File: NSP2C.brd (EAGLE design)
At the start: 72.1 x 82.5 mm, 15 parts, among them Q1 600mA/40V, Q2 IRF540

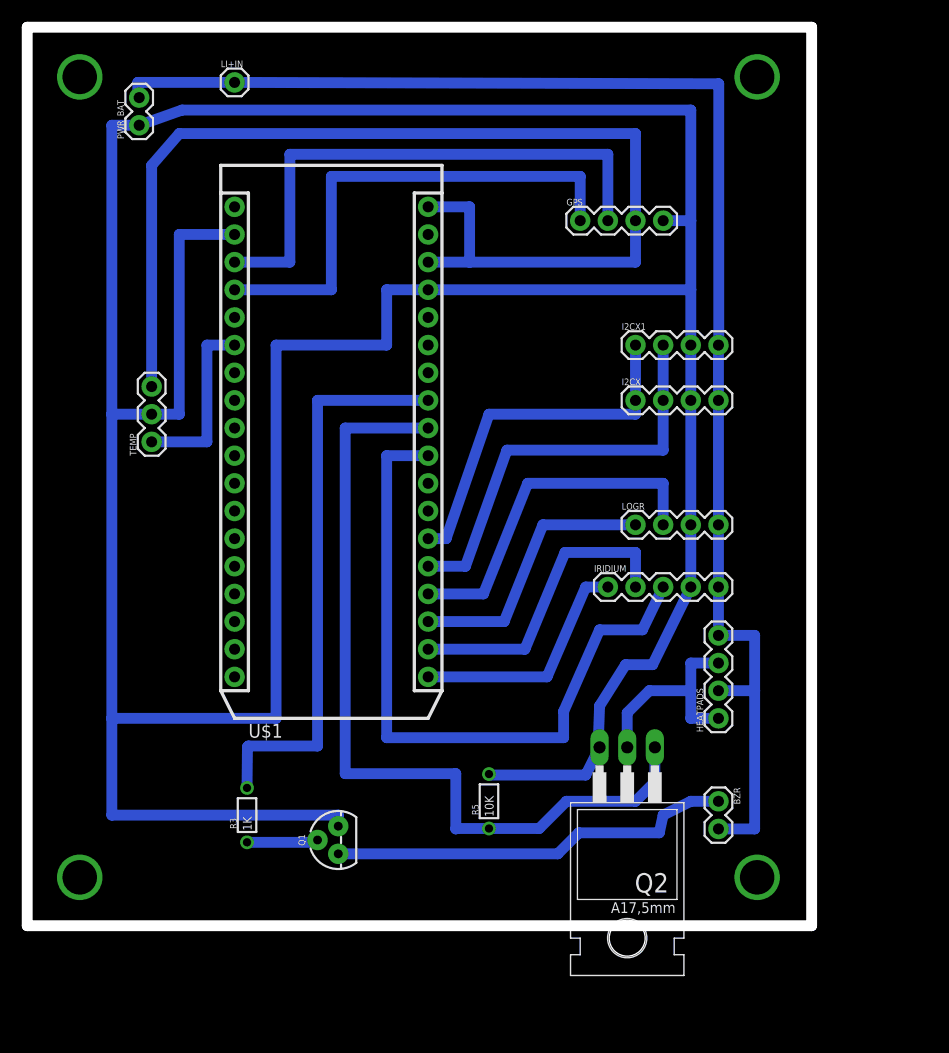
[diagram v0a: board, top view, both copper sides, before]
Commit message: Improved routing
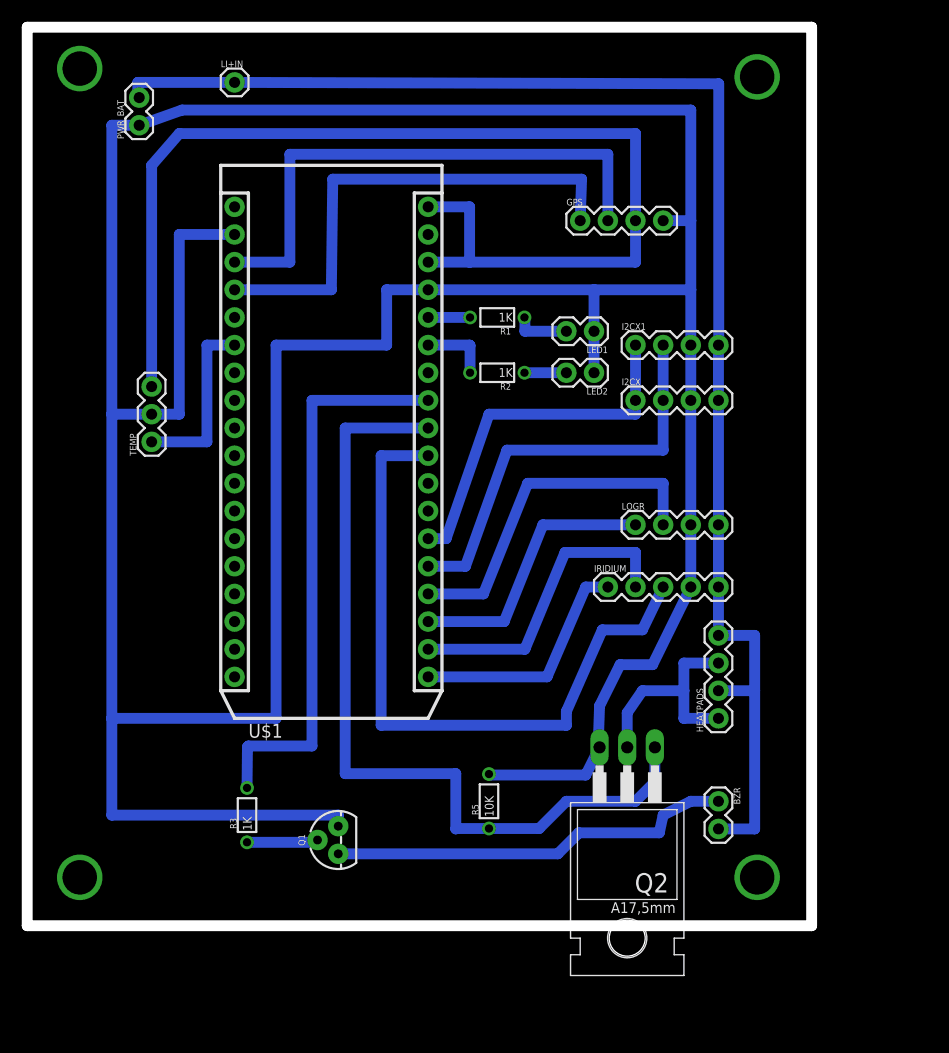
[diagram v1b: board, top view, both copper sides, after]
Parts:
- added LED1, LED2: (no value), SparkFun-Connectors:1X02
- added R1, R2: 1K, SparkFun-Passives:1/6W-RES
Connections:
- new net N$13: R2.2, U$1.31
- new net N$16: LED2.2, R2.1
- new net N$3: R1.2, U$1.32
- new net N$8: LED1.2, R1.1
- net GND: now also LED1.1, LED2.1
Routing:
- net GND: track 336.8 -> 344.6 mm
- net N$13: track 0.00 -> 6.37 mm
- net N$8: track 0.00 -> 5.10 mm
- net N$3: track 0.00 -> 3.85 mm
- net N$16: track 0.00 -> 3.85 mm
- net IRWKP: track 64.9 -> 63.6 mm
- net N$11: track 20.1 -> 21.0 mm
- net N$12: track 46.2 -> 45.7 mm
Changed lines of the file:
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@@
 <element name="Q2" library="transistor-fet" library_urn="urn:adsk.eagle:library:396" package="TO220" package3d_urn="urn:adsk.eagle:package:28520/1" value="IRF540" x="44.958" y="15.113" rot="R180"/>
 <element name="R5" library="SparkFun-Passives" package="1/6W-RES" value="10K" x="32.258" y="16.51" rot="R90"/>
+<element name="R1" library="SparkFun-Passives" package="1/6W-RES" value="1K" x="33.02" y="60.96" rot="R180"/>
+<element name="LED1" library="SparkFun-Connectors" package="1X02" value="" x="41.91" y="59.69" rot="R180"/>
+<element name="LED2" library="SparkFun-Connectors" package="1X02" value="" x="41.91" y="55.88" rot="R180"/>
+<element name="R2" library="SparkFun-Passives" package="1/6W-RES" value="1K" x="33.02" y="55.88" rot="R180"/>
 </elements>
 <signals>
@@
 <wire x1="12.7" y1="24.13" x2="-2.3876" y2="24.13" width="1" layer="16"/>
 <wire x1="22.86" y1="63.5" x2="26.67" y2="63.5" width="1" layer="16"/>
-<wire x1="26.67" y1="63.5" x2="50.8" y2="63.5" width="1" layer="16"/>
+<wire x1="41.91" y1="63.5" x2="50.8" y2="63.5" width="1" layer="16"/>
+<wire x1="41.91" y1="63.5" x2="26.67" y2="63.5" width="1" layer="16"/>
 <wire x1="50.8" y1="63.5" x2="50.8" y2="69.85" width="1" layer="16"/>
 <contactref element="GPS" pad="4"/>
@@
 <wire x1="0.127" y1="78.613" x2="-2.3876" y2="78.613" width="1" layer="16"/>
 <wire x1="-2.3876" y1="78.613" x2="-2.3876" y2="52.07" width="1" layer="16"/>
-<wire x1="47.291765625" y1="29.061590625" x2="44.809590625" y2="29.061590625" width="1" layer="16"/>
-<wire x1="44.809590625" y1="29.061590625" x2="42.418" y2="25.273" width="1" layer="16"/>
+<wire x1="47.291765625" y1="29.061590625" x2="44.301590625" y2="29.061590625" width="1" layer="16"/>
+<wire x1="44.301590625" y1="29.061590625" x2="42.418" y2="25.273" width="1" layer="16"/>
 <wire x1="42.418" y1="25.273" x2="42.291" y2="21.59" width="1" layer="16"/>
 <wire x1="42.291" y1="21.59" x2="42.418" y2="21.463" width="1" layer="16"/>
+<contactref element="LED1" pad="1"/>
+<contactref element="LED2" pad="1"/>
+<wire x1="41.91" y1="55.88" x2="41.91" y2="59.69" width="1" layer="16"/>
+<wire x1="41.91" y1="59.69" x2="41.91" y2="63.5" width="1" layer="16"/>
 </signal>
 <signal name="3.3V">
@@
 <contactref element="U$1" pad="27"/>
 <contactref element="IRIDIUM" pad="3"/>
-<wire x1="26.67" y1="48.26" x2="22.86" y2="48.26" width="1" layer="16"/>
-<wire x1="22.86" y1="48.26" x2="22.86" y2="22.352" width="1" layer="16"/>
-<wire x1="22.86" y1="22.352" x2="39.116" y2="22.352" width="1" layer="16"/>
+<wire x1="26.67" y1="48.26" x2="22.352" y2="48.26" width="1" layer="16"/>
+<wire x1="22.352" y1="48.26" x2="22.352" y2="23.495" width="1" layer="16"/>
+<wire x1="22.352" y1="23.495" x2="39.37" y2="23.495" width="1" layer="16"/>
 <wire x1="46.355" y1="32.258" x2="48.26" y2="36.195" width="1" layer="16"/>
-<wire x1="39.116" y1="22.352" x2="39.116" y2="24.765" width="1" layer="16"/>
-<wire x1="39.116" y1="24.765" x2="42.418" y2="32.258" width="1" layer="16"/>
-<wire x1="42.418" y1="32.258" x2="46.355" y2="32.258" width="1" layer="16"/>
+<wire x1="39.37" y1="23.495" x2="39.37" y2="24.765" width="1" layer="16"/>
+<wire x1="39.37" y1="24.765" x2="42.672" y2="32.258" width="1" layer="16"/>
+<wire x1="42.672" y1="32.258" x2="46.355" y2="32.258" width="1" layer="16"/>
 </signal>
 <signal name="SDA">
@@
 <contactref element="U$1" pad="29"/>
 <contactref element="R3" pad="2"/>
-<wire x1="26.67" y1="53.34" x2="16.51" y2="53.34" width="1" layer="16"/>
-<wire x1="16.51" y1="53.34" x2="16.51" y2="21.59" width="1" layer="16"/>
-<wire x1="16.51" y1="21.59" x2="10.16" y2="21.59" width="1" layer="16"/>
+<wire x1="26.67" y1="53.34" x2="16.002" y2="53.34" width="1" layer="16"/>
+<wire x1="16.002" y1="53.34" x2="16.002" y2="21.59" width="1" layer="16"/>
+<wire x1="16.002" y1="21.59" x2="10.16" y2="21.59" width="1" layer="16"/>
 <wire x1="10.16" y1="21.59" x2="10.073" y2="21.503" width="1" layer="16"/>
 <wire x1="10.073" y1="21.503" x2="10.033" y2="17.74" width="1" layer="16"/>
@@
 <contactref element="HEATPADS" pad="1"/>
 <contactref element="HEATPADS" pad="3"/>
-<wire x1="50.8" y1="29.21" x2="53.34" y2="29.21" width="1" layer="16"/>
-<wire x1="50.8" y1="29.21" x2="50.8" y2="26.67" width="1" layer="16"/>
-<wire x1="50.8" y1="26.67" x2="50.8" y2="24.13" width="1" layer="16"/>
-<wire x1="50.8" y1="24.13" x2="53.34" y2="24.13" width="1" layer="16"/>
+<wire x1="50.165" y1="29.21" x2="53.34" y2="29.21" width="1" layer="16"/>
+<wire x1="50.165" y1="29.21" x2="50.165" y2="26.67" width="1" layer="16"/>
+<wire x1="50.165" y1="26.67" x2="50.165" y2="24.13" width="1" layer="16"/>
+<wire x1="50.165" y1="24.13" x2="53.34" y2="24.13" width="1" layer="16"/>
 <wire x1="45.085" y1="21.59" x2="44.958" y2="21.463" width="1" layer="16"/>
-<wire x1="50.8" y1="26.67" x2="46.99" y2="26.67" width="1" layer="16"/>
-<wire x1="46.99" y1="26.67" x2="44.958" y2="24.638" width="1" layer="16"/>
+<wire x1="50.165" y1="26.67" x2="46.355" y2="26.67" width="1" layer="16"/>
+<wire x1="46.355" y1="26.67" x2="44.958" y2="24.638" width="1" layer="16"/>
 <wire x1="44.958" y1="21.717" x2="45.085" y2="21.59" width="1" layer="16"/>
 <wire x1="44.958" y1="24.638" x2="44.958" y2="21.717" width="1" layer="16"/>
@@
 <contactref element="GPS" pad="1"/>
 <wire x1="8.89" y1="63.5" x2="17.78" y2="63.5" width="1" layer="16"/>
-<wire x1="17.78" y1="63.5" x2="17.78" y2="73.914" width="1" layer="16"/>
-<wire x1="17.78" y1="73.914" x2="40.64" y2="73.914" width="1" layer="16"/>
-<wire x1="40.64" y1="73.914" x2="40.64" y2="69.85" width="1" layer="16"/>
+<wire x1="17.78" y1="63.5" x2="17.907" y2="73.66" width="1" layer="16"/>
+<wire x1="17.907" y1="73.66" x2="40.767" y2="73.66" width="1" layer="16"/>
+<wire x1="40.767" y1="73.66" x2="40.64" y2="69.85" width="1" layer="16"/>
 </signal>
 <signal name="N$14">
@@
 <signal name="N$4">
 <via x="56.896" y="83.058" extent="1-16" drill="3.17"/>
-<via x="-5.334" y="83.058" extent="1-16" drill="3.17"/>
 </signal>
 <signal name="N$5">
@@
 <via x="-5.334" y="9.525" extent="1-16" drill="3.17"/>
 </signal>
+<signal name="N$3">
+<contactref element="U$1" pad="32"/>
+<contactref element="R1" pad="2"/>
+<wire x1="26.67" y1="60.96" x2="30.52" y2="60.96" width="1" layer="16"/>
+</signal>
+<signal name="N$8">
+<contactref element="R1" pad="1"/>
+<contactref element="LED1" pad="2"/>
+<wire x1="35.52" y1="60.96" x2="35.56" y2="60.92" width="1" layer="16"/>
+<wire x1="35.56" y1="60.92" x2="35.56" y2="59.69" width="1" layer="16"/>
+<wire x1="35.56" y1="59.69" x2="39.37" y2="59.69" width="1" layer="16"/>
+</signal>
+<signal name="N$13">
+<contactref element="U$1" pad="31"/>
+<contactref element="R2" pad="2"/>
+<wire x1="26.67" y1="58.42" x2="30.48" y2="58.42" width="1" layer="16"/>
+<wire x1="30.48" y1="58.42" x2="30.52" y2="58.38" width="1" layer="16"/>
+<wire x1="30.52" y1="58.38" x2="30.52" y2="55.88" width="1" layer="16"/>
+</signal>
+<signal name="N$16">
+<contactref element="R2" pad="1"/>
+<contactref element="LED2" pad="2"/>
+<wire x1="39.37" y1="55.88" x2="35.52" y2="55.88" width="1" layer="16"/>
+</signal>
+<signal name="N$17">
+<via x="-5.334" y="83.82" extent="1-16" drill="3.17"/>
+</signal>
 </signals>

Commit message: Added capacitor for batt source
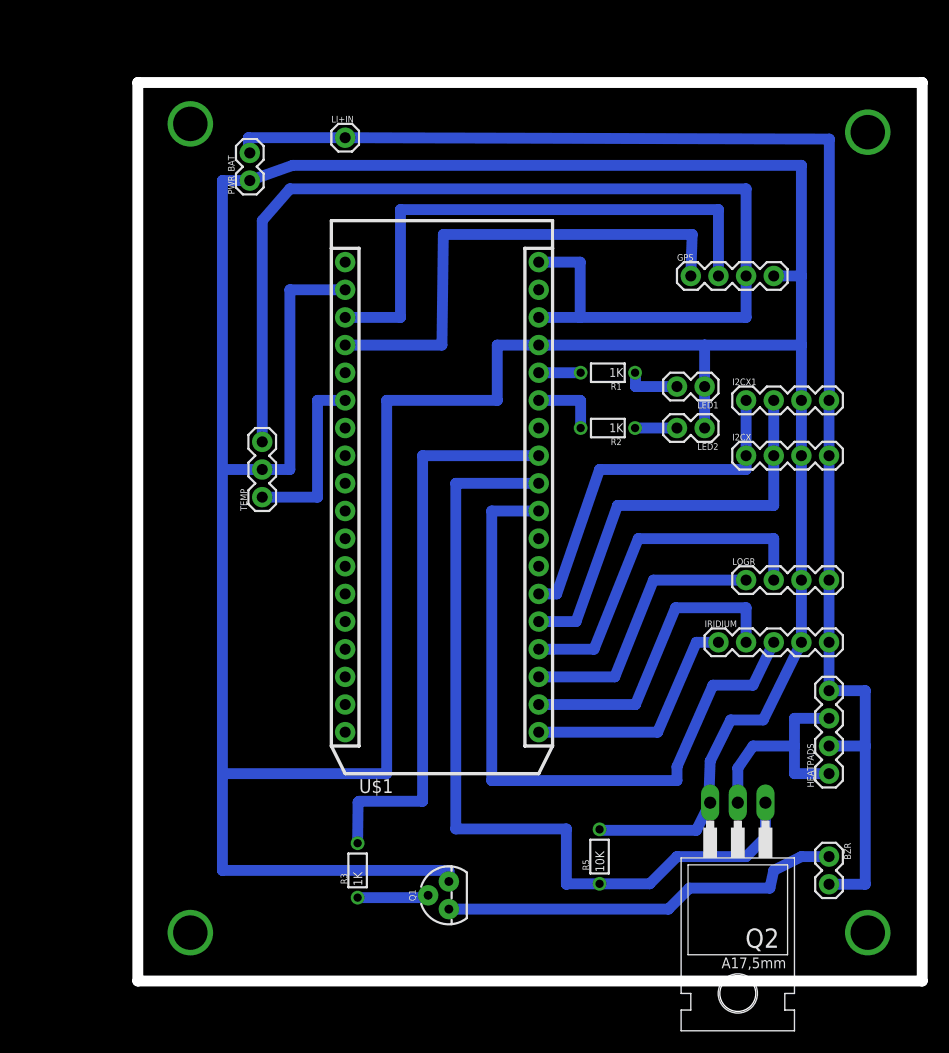
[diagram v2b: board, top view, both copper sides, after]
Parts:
- moved I2CX 11.4 mm to (55.9, 48.3)
- moved LED2 11.4 mm to (52.1, 50.8)
- moved IRIDIUM 11.4 mm to (53.3, 31.1)
- moved I2CX1 11.4 mm to (55.9, 53.3)
- moved LED1 11.4 mm to (52.1, 54.6)
- moved LOGR 11.4 mm to (55.9, 36.8)
- moved Q2 11.4 mm to (55.1, 10.0)
- moved R3 11.4 mm to (20.2, 10.2)
- moved Q1 11.4 mm to (28.6, 7.87)
- moved BZR 11.4 mm to (63.5, 11.4)
- moved R2 11.4 mm to (43.2, 50.8)
- moved R5 11.4 mm to (42.4, 11.4)
- moved LI+IN 11.4 mm to (19.1, 77.5)
- moved PWR_BAT 11.4 mm to (10.3, 73.5)
- moved TEMP 11.4 mm to (11.4, 44.5)
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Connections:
- net N$10 renamed BASE
- net N$12 renamed RX
- net N$2 renamed TX
